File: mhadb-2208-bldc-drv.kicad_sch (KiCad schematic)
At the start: 69 parts, among them J1 TC2030, J2 Conn_01x04_Pin, J3 Conn_01x04, M2 Motor_3_Phases, SW1 SW_Push, SW2 SW_Push, SW4 SW_Push, U1 AS5600-ASOT, U10 DRV8311H, U2 SN65HVD230, U3 STM32F103C8Tx, Y1 8M

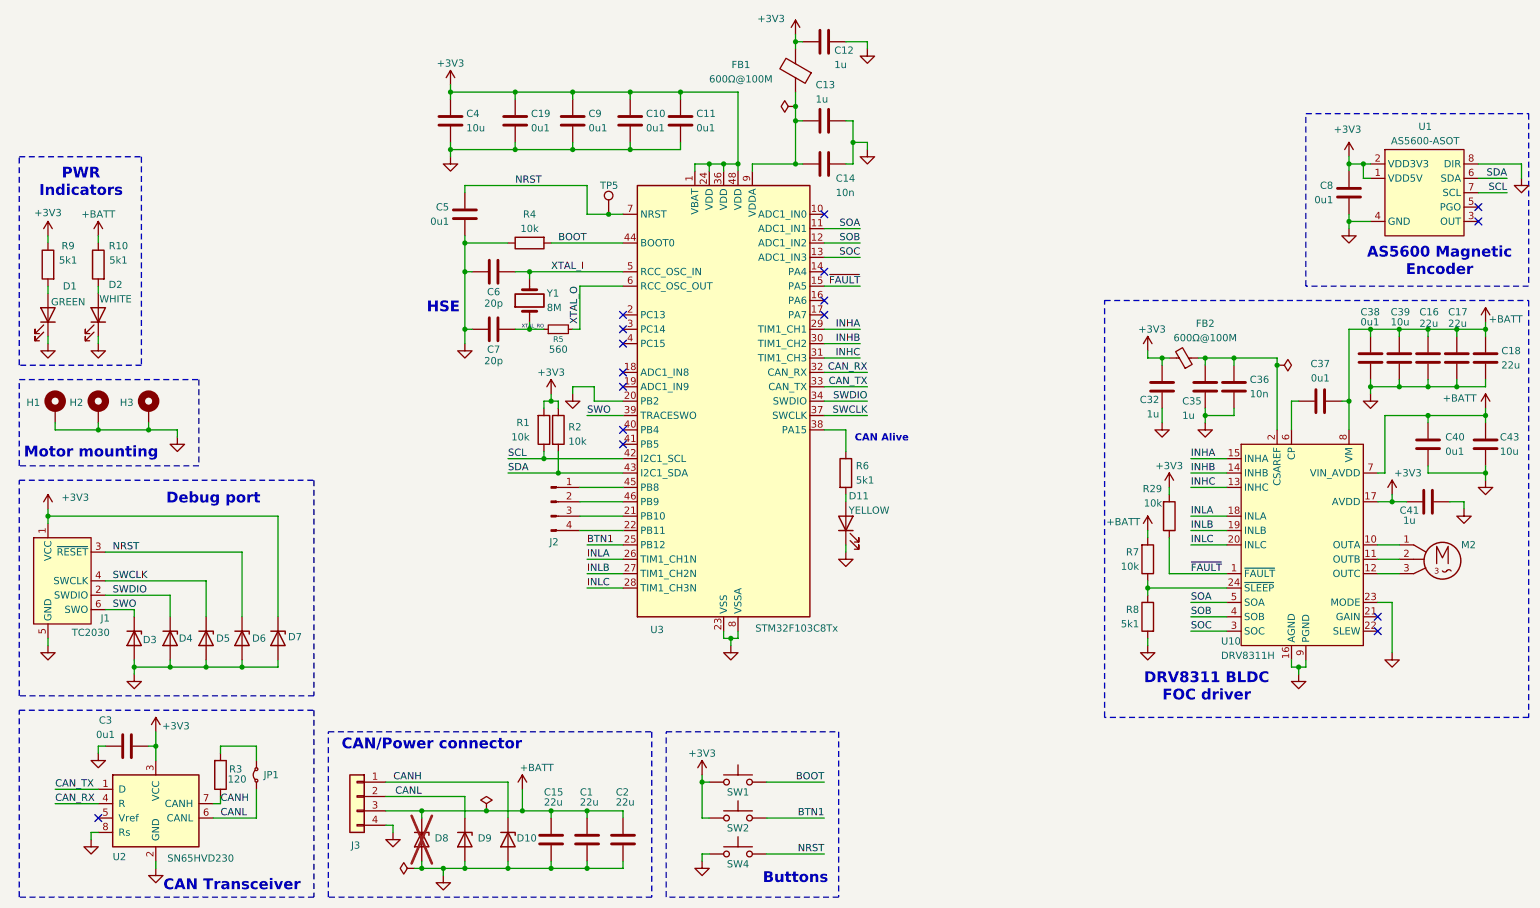
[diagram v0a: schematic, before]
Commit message: schem: renumber
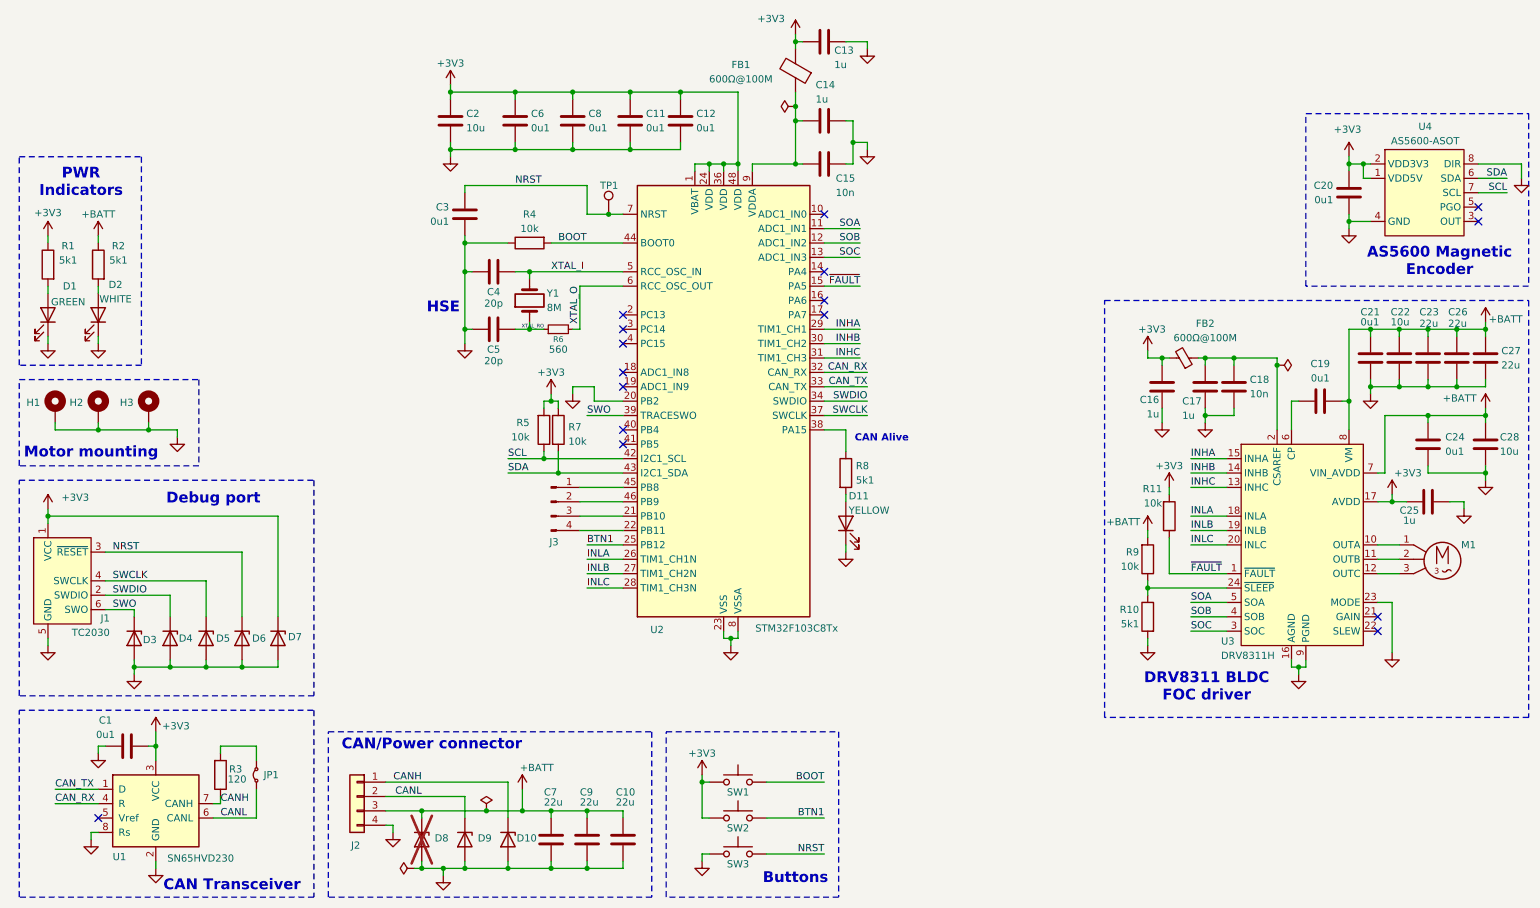
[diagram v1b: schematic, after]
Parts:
- renumbered C3 to C1, C2 to C10, C10 to C11, C11 to C12, C12 to C13, C13 to C14, C14 to C15, C32 to C16, C35 to C17, C36 to C18, C37 to C19, C4 to C2, C8 to C20, C38 to C21, C39 to C22, C16 to C23, C40 to C24, C41 to C25, C17 to C26, C18 to C27, C43 to C28, C5 to C3, C6 to C4, C7 to C5, C19 to C6, C15 to C7, C9 to C8, C1 to C9, J3 to J2, J2 to J3, M2 to M1, R9 to R1, R8 to R10, R29 to R11, R10 to R2, R1 to R5, R5 to R6, R2 to R7, R6 to R8, R7 to R9, SW4 to SW3, TP5 to TP1, U2 to U1, U3 to U2, U10 to U3, U1 to U4

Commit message: schem: add title
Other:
- company: (none) -> Mechadiabatik
- title: (none) -> MHADB BLDC Driver
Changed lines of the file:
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@@
 	(generator_version "9.0")
 	(paper "A4")
+	(title_block
+		(title "MHADB BLDC Driver")
+		(date "2026-01-10")
+		(rev "01")
+		(company "Mechadiabatik")
+	)
 	(rectangle
 		(start 207.01 88.9)

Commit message: pcb: update from schema
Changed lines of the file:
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@@
 	(wire
 		(pts
-			(xy 280.67 64.77) (xy 273.05 64.77)
+			(xy 279.4 64.77) (xy 273.05 64.77)
 		)
 		(stroke
@@
 	(wire
 		(pts
-			(xy 280.67 64.77) (xy 280.67 67.31)
+			(xy 279.4 64.77) (xy 279.4 71.12)
 		)
 		(stroke
@@
 	(symbol
 		(lib_id "power:GND")
-		(at 280.67 67.31 0)
+		(at 279.4 71.12 0)
 		(unit 1)
 		(exclude_from_sim no)
@@
 		(fields_autoplaced yes)
 		(property "Reference" "#PWR044"
-			(at 280.67 73.66 0)
+			(at 279.4 77.47 0)
 			(effects
 				(font
@@
 		)
 		(property "Value" "GND"
-			(at 280.67 72.39 0)
+			(at 279.4 76.2 0)
 			(effects
 				(font
@@
 		)
 		(property "Footprint" ""
-			(at 280.67 67.31 0)
+			(at 279.4 71.12 0)
 			(effects
 				(font
@@
 		)
 		(property "Datasheet" ""
-			(at 280.67 67.31 0)
+			(at 279.4 71.12 0)
 			(effects
 				(font
@@
 		)
 		(property "Description" "Power symbol creates a global label with name \"GND\" , ground"
-			(at 280.67 67.31 0)
+			(at 279.4 71.12 0)
 			(effects
 				(font
@@
 		(dnp no)
 		(property "Reference" "C22"
-			(at 257.556 90.932 0)
+			(at 257.556 90.678 0)
 			(effects
 				(font
@@
 		)
 		(property "Value" "10u"
-			(at 257.556 92.71 0)
+			(at 257.556 92.456 0)
 			(effects
 				(font
@@
 		(dnp no)
 		(property "Reference" "C26"
-			(at 267.716 90.932 0)
+			(at 267.716 90.678 0)
 			(effects
 				(font
@@
 		)
 		(property "Value" "22u"
-			(at 267.716 92.964 0)
+			(at 267.716 92.71 0)
 			(effects
 				(font
@@
 		(dnp no)
 		(property "Reference" "C23"
-			(at 262.636 90.932 0)
+			(at 262.636 90.678 0)
 			(effects
 				(font
@@
 		)
 		(property "Value" "22u"
-			(at 262.636 92.964 0)
+			(at 262.636 92.71 0)
 			(effects
 				(font
@@
 		(dnp no)
 		(property "Reference" "C21"
-			(at 252.222 90.932 0)
+			(at 252.222 90.678 0)
 			(effects
 				(font
@@
 		)
 		(property "Value" "0u1"
-			(at 252.222 92.71 0)
+			(at 252.222 92.456 0)
 			(effects
 				(font

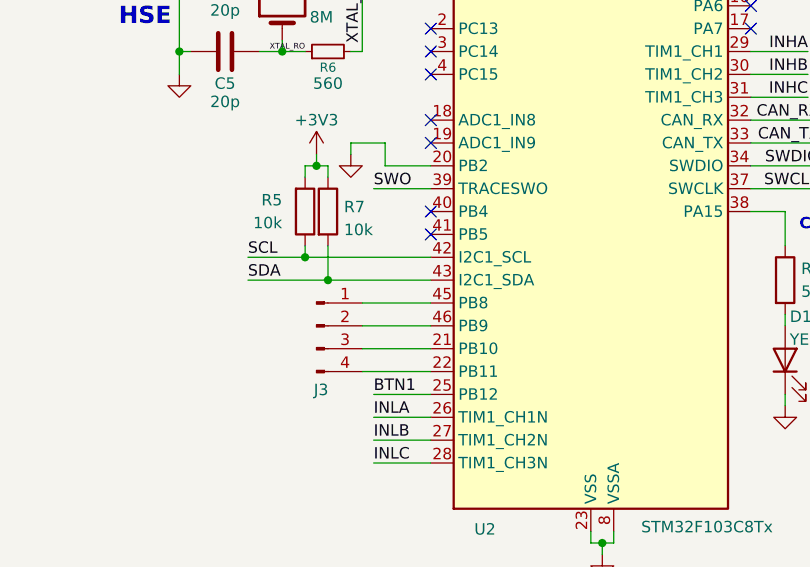
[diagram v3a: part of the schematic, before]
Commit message: pcb: route crystal
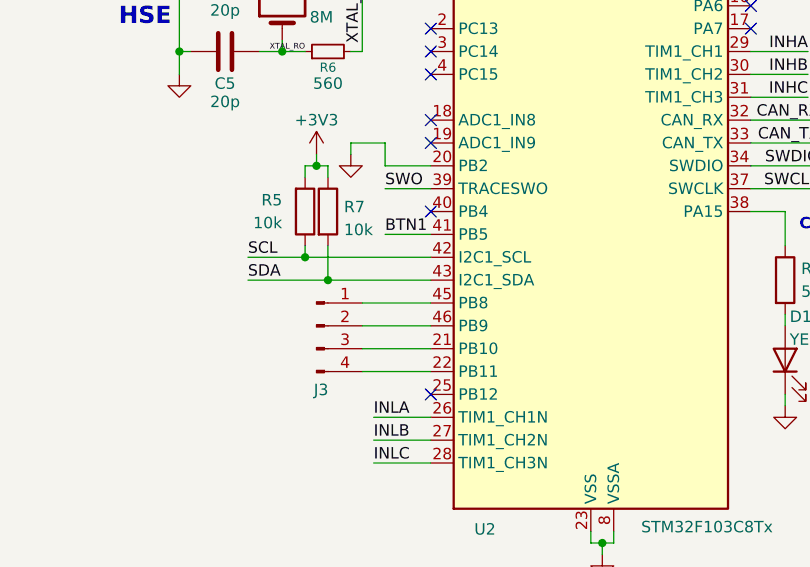
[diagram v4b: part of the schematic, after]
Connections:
- net BTN1: now also U2.41 (PB5); no longer U2.25 (PB12)
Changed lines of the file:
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@@
 	)
 	(no_connect
+		(at 121.92 111.76)
+	)
+	(no_connect
+		(at 121.92 132.08)
+	)
+	(no_connect
 		(at 121.92 101.6)
 	)
@@
 	)
 	(no_connect
-		(at 121.92 114.3)
-	)
-	(no_connect
 		(at 157.48 91.44)
 	)
@@
 	)
 	(no_connect
-		(at 121.92 111.76)
-	)
-	(no_connect
 		(at 157.48 83.82)
 	)
@@
 	(wire
 		(pts
+			(xy 116.84 114.3) (xy 121.92 114.3)
+		)
+		(stroke
+			(width 0)
+			(type default)
+		)
+	)
+	(wire
+		(pts
 			(xy 139.7 148.59) (xy 139.7 147.32)
 		)
@@
 	(wire
 		(pts
-			(xy 115.57 109.22) (xy 121.92 109.22)
+			(xy 116.84 109.22) (xy 121.92 109.22)
 		)
 		(stroke
@@
 	(wire
 		(pts
-			(xy 115.57 132.08) (xy 121.92 132.08)
-		)
-		(stroke
-			(width 0)
-			(type default)
-		)
-	)
-	(wire
-		(pts
 			(xy 224.79 109.22) (xy 224.79 107.95)
 		)
@@
 		)
 	)
+	(label "BTN1"
+		(at 116.84 114.3 0)
+		(effects
+			(font
+				(size 1.27 1.27)
+			)
+			(justify left bottom)
+		)
+	)
 	(label "BOOT"
 		(at 157.48 173.99 180)
@@
 	)
 	(label "SWO"
-		(at 115.57 109.22 0)
+		(at 116.84 109.22 0)
 		(effects
 			(font
@@
 		(effects
 			(font
-				(size 1.27 1.27)
-			)
-			(justify left bottom)
-		)
-	)
-	(label "BTN1"
-		(at 115.57 132.08 0)
-		(effects
-			(font

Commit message: update BOM
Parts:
- FB1: Basic Y -> X; JLCPCB Part # C1015 -> C81034; Manufacturer Sunlord -> TDK; Manufacturer Part Number GZ2012D101TF -> MPZ2012S601ATD25
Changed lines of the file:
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@@
 			)
 		)
-		(property "Basic" "Y"
+		(property "Basic" "X"
 			(at 152.4 48.26 0)
 			(effects
@@
 			)
 		)
-		(property "JLCPCB Part #" "C1015"
+		(property "JLCPCB Part #" "C81034"
 			(at 152.4 48.26 0)
 			(effects
@@
 			)
 		)
-		(property "Manufacturer" "Sunlord"
+		(property "Manufacturer" "TDK"
 			(at 152.4 48.26 0)
 			(effects
@@
 			)
 		)
-		(property "Manufacturer Part Number" "GZ2012D101TF"
+		(property "Manufacturer Part Number" "MPZ2012S601ATD25"
 			(at 152.4 48.26 0)
 			(effects
